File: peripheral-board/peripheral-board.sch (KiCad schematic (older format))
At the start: 12 parts, among them CON1001 AVR-ISP-10, P1001 Peripheral Bus, P1002 Power, SW1001 Power, U1001 ATTINY48-A

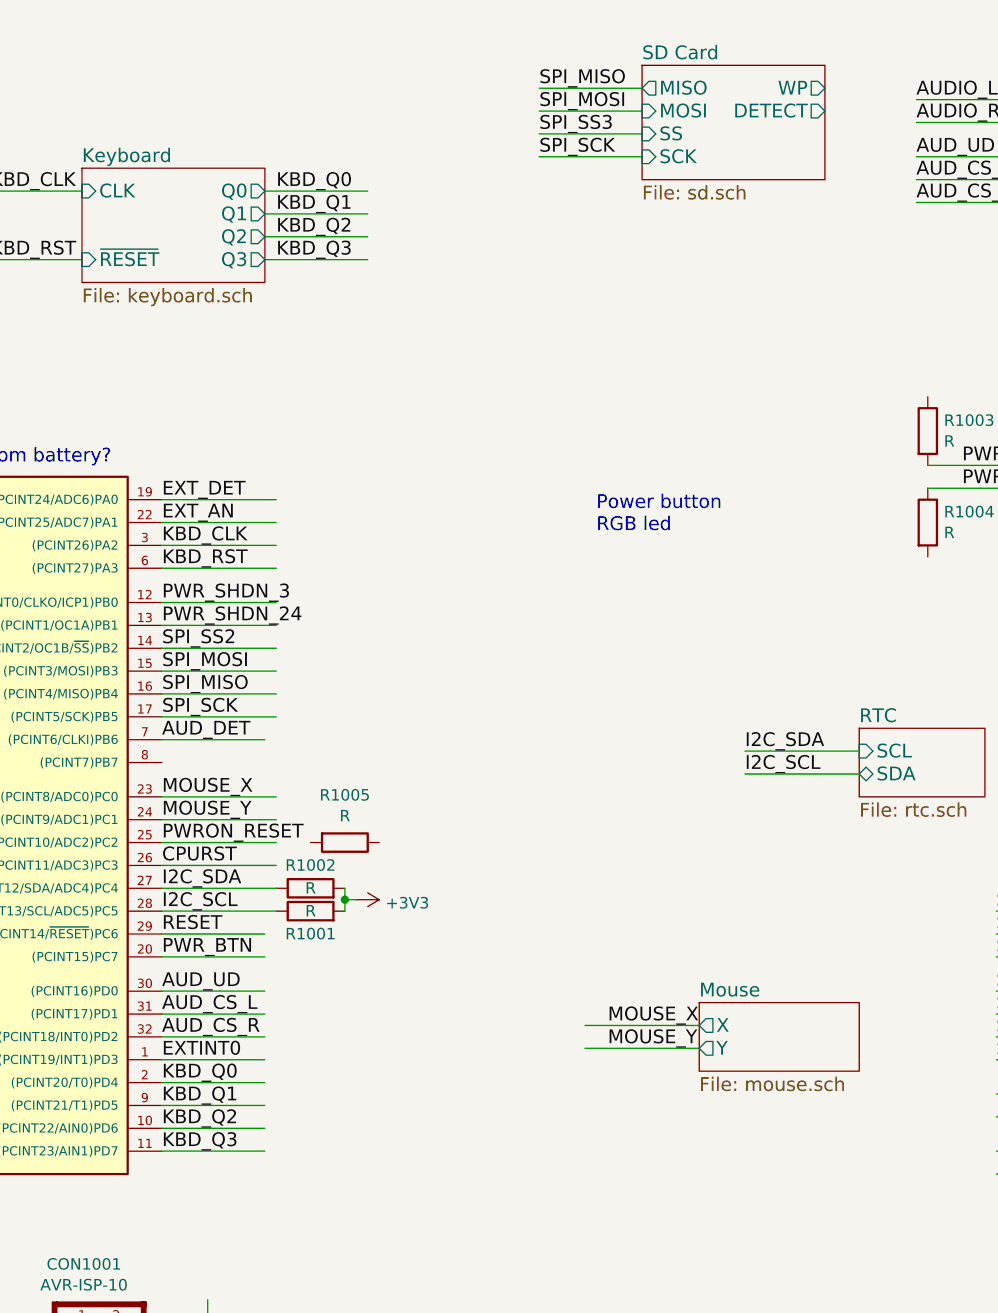
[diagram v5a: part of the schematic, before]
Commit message: audio components placement
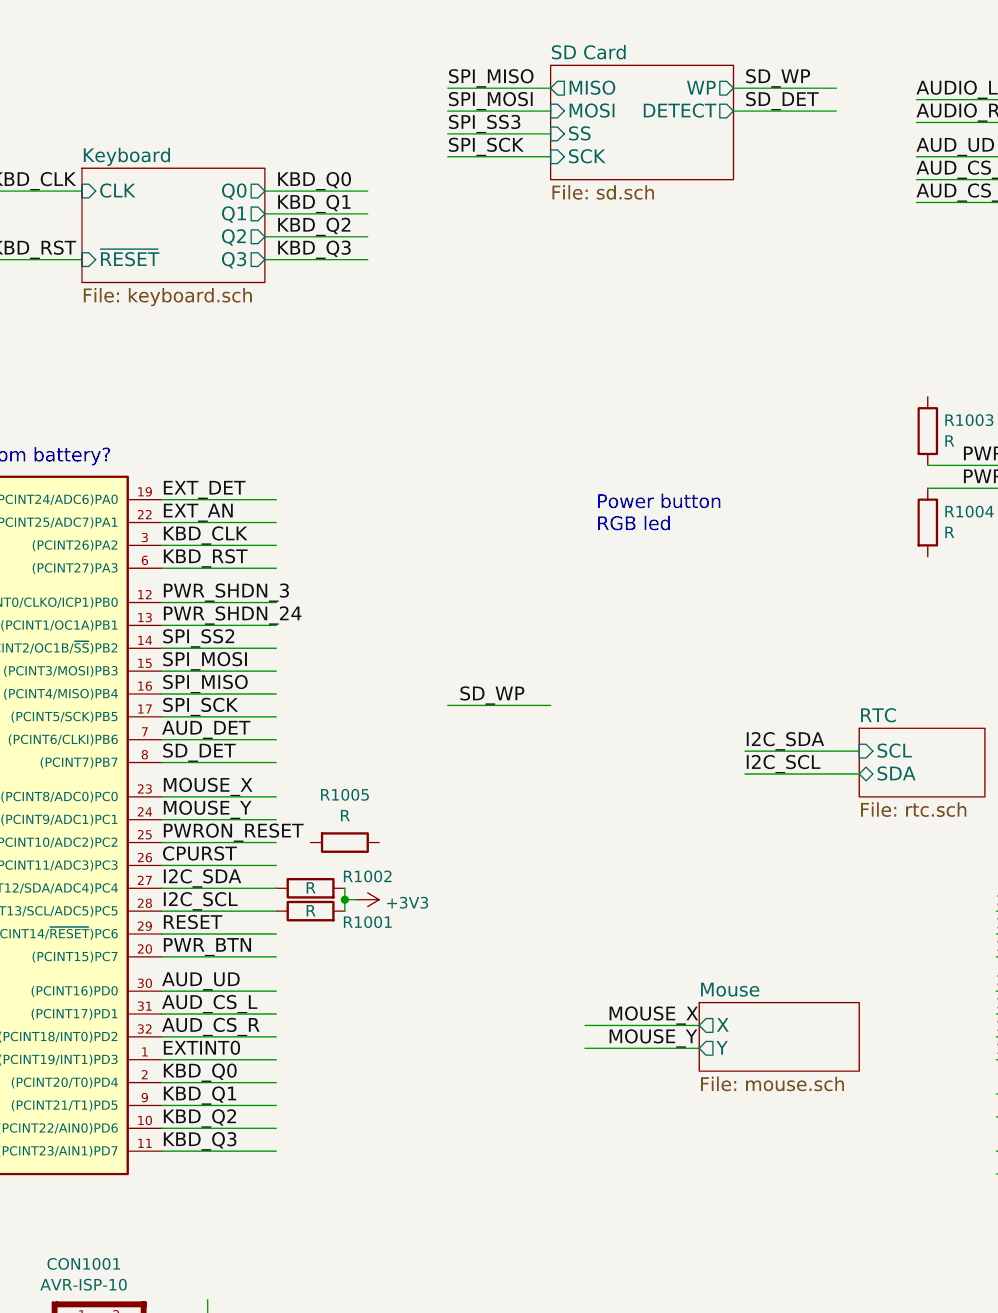
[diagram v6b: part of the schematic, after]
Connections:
- net labels added: SD_DET, SD_WP
- wire segments 126 -> 130
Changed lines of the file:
@@
 SPI_SCK
 $Comp
-L GND #PWR1014
+L GND #PWR01
 U 1 1 581F4F29
 P 5150 6850
-F 0 "#PWR1014" H 5150 6600 50  0001 C CNN
+F 0 "#PWR01" H 5150 6600 50  0001 C CNN
 F 1 "GND" H 5155 6677 50  0000 C CNN
 F 2 "" H 5150 6850 50  0000 C CNN
@@
 NoConn ~ 4550 6500
 $Comp
-L GND #PWR1011
+L GND #PWR02
 U 1 1 581F524B
 P 3000 5700
-F 0 "#PWR1011" H 3000 5450 50  0001 C CNN
+F 0 "#PWR02" H 3000 5450 50  0001 C CNN
 F 1 "GND" H 3005 5527 50  0000 C CNN
 F 2 "" H 3000 5700 50  0000 C CNN
@@
 SPI_SS7
 $Comp
-L GND #PWR1001
+L GND #PWR03
 U 1 1 581F752E
 P 1000 1950
-F 0 "#PWR1001" H 1000 1700 50  0001 C CNN
+F 0 "#PWR03" H 1000 1700 50  0001 C CNN
 F 1 "GND" V 1005 1822 50  0000 R CNN
 F 2 "" H 1000 1950 50  0000 C CNN
@@
 $EndComp
 $Comp
-L GND #PWR1002
+L GND #PWR04
 U 1 1 581F7634
 P 1000 2800
-F 0 "#PWR1002" H 1000 2550 50  0001 C CNN
+F 0 "#PWR04" H 1000 2550 50  0001 C CNN
 F 1 "GND" V 1005 2672 50  0000 R CNN
 F 2 "" H 1000 2800 50  0000 C CNN
@@
 $EndComp
 $Comp
-L GND #PWR1003
+L GND #PWR05
 U 1 1 581F76B8
 P 1000 3200
-F 0 "#PWR1003" H 1000 2950 50  0001 C CNN
+F 0 "#PWR05" H 1000 2950 50  0001 C CNN
 F 1 "GND" V 1005 3072 50  0000 R CNN
 F 2 "" H 1000 3200 50  0000 C CNN
@@
 $EndComp
 $Comp
-L GND #PWR1004
+L GND #PWR06
 U 1 1 581F7709
 P 1000 3500
-F 0 "#PWR1004" H 1000 3250 50  0001 C CNN
+F 0 "#PWR06" H 1000 3250 50  0001 C CNN
 F 1 "GND" V 1005 3372 50  0000 R CNN
 F 2 "" H 1000 3500 50  0000 C CNN
@@
 $EndComp
 $Comp
-L GND #PWR1005
+L GND #PWR07
 U 1 1 581F7744
 P 1000 4200
-F 0 "#PWR1005" H 1000 3950 50  0001 C CNN
+F 0 "#PWR07" H 1000 3950 50  0001 C CNN
 F 1 "GND" V 1005 4072 50  0000 R CNN
 F 2 "" H 1000 4200 50  0000 C CNN
@@
 $EndComp
 $Comp
-L GND #PWR1006
+L GND #PWR08
 U 1 1 581F77D7
 P 1000 4450
-F 0 "#PWR1006" H 1000 4200 50  0001 C CNN
+F 0 "#PWR08" H 1000 4200 50  0001 C CNN
 F 1 "GND" V 1005 4322 50  0000 R CNN
 F 2 "" H 1000 4450 50  0000 C CNN
@@
 $EndComp
 $Comp
-L GND #PWR1009
+L GND #PWR09
 U 1 1 581F7812
 P 1000 4950
-F 0 "#PWR1009" H 1000 4700 50  0001 C CNN
+F 0 "#PWR09" H 1000 4700 50  0001 C CNN
 F 1 "GND" V 1005 4822 50  0000 R CNN
 F 2 "" H 1000 4950 50  0000 C CNN
@@
 $EndComp
 $Comp
-L +24V #PWR1008
+L +24V #PWR010
 U 1 1 581F7F97
 P 1000 4800
-F 0 "#PWR1008" H 1000 4650 50  0001 C CNN
+F 0 "#PWR010" H 1000 4650 50  0001 C CNN
 F 1 "+24V" V 1000 4950 50  0000 L CNN
 F 2 "" H 1000 4800 50  0000 C CNN
@@
 $EndComp
 $Comp
-L +3V3 #PWR1010
+L +3V3 #PWR011
 U 1 1 581F7FED
 P 1000 5100
-F 0 "#PWR1010" H 1000 4950 50  0001 C CNN
+F 0 "#PWR011" H 1000 4950 50  0001 C CNN
 F 1 "+3V3" V 1000 5250 50  0000 L CNN
 F 2 "" H 1000 5100 50  0000 C CNN
@@
 $EndComp
 $Sheet
-S 7050 900  800  500
+S 6650 900  800  500
 U 581F67DF
 F0 "SD Card" 60
 F1 "sd.sch" 60
-F2 "MISO" O L 7050 1000 60
-F3 "MOSI" I L 7050 1100 60
-F4 "SS" I L 7050 1200 60
-F5 "SCK" I L 7050 1300 60
-F6 "WP" O R 7850 1000 60
-F7 "DETECT" O R 7850 1100 60
+F2 "MISO" O L 6650 1000 60
+F3 "MOSI" I L 6650 1100 60
+F4 "SS" I L 6650 1200 60
+F5 "SCK" I L 6650 1300 60
+F6 "WP" O R 7450 1000 60
+F7 "DETECT" O R 7450 1100 60
 $EndSheet
 $Comp
@@
 $EndComp
 $Comp
-L GND #PWR1013
+L GND #PWR012
 U 1 1 581F76DB
 P 2700 6850
-F 0 "#PWR1013" H 2700 6600 50  0001 C CNN
+F 0 "#PWR012" H 2700 6600 50  0001 C CNN
 F 1 "GND" H 2705 6677 50  0000 C CNN
 F 2 "" H 2700 6850 50  0000 C CNN
@@
 $EndComp
 $Comp
-L +3V3 #PWR1012
+L +3V3 #PWR013
 U 1 1 581F7984
 P 2700 6400
-F 0 "#PWR1012" H 2700 6250 50  0001 C CNN
+F 0 "#PWR013" H 2700 6250 50  0001 C CNN
 F 1 "+3V3" H 2715 6573 50  0000 C CNN
 F 2 "" H 2700 6400 50  0000 C CNN
@@
 U 1 1 58224307
 P 5600 4600
-F 0 "R1001" V 5500 4600 50  0000 C CNN
+F 0 "R1001" V 5550 4350 50  0000 C CNN
 F 1 "R" V 5600 4600 50  0000 C CNN
 F 2 "Resistors_SMD:R_0805" V 5530 4600 50  0001 C CNN
@@
 U 1 1 582244B8
 P 5600 4500
-F 0 "R1002" V 5700 4500 50  0000 C CNN
+F 0 "R1002" V 5650 4250 50  0000 C CNN
 F 1 "R" V 5600 4500 50  0000 C CNN
 F 2 "Resistors_SMD:R_0805" V 5530 4500 50  0001 C CNN
@@
 I2C_SCL
 $Comp
-L +3V3 #PWR1007
+L +3V3 #PWR014
 U 1 1 58A469F7
 P 5800 4550
-F 0 "#PWR1007" H 5850 4600 50  0001 C CNN
+F 0 "#PWR014" H 5850 4600 50  0001 C CNN
 F 1 "+3V3" V 5815 4678 50  0000 L CNN
 F 2 "" H -500 0   50  0001 C CNN
@@
 Text Label 4200 1750 0    60   ~ 0
 KBD_RST
-Text Label 6600 1100 0    60   ~ 0
+Text Label 6200 1100 0    60   ~ 0
 SPI_MOSI
-Text Label 6600 1000 0    60   ~ 0
+Text Label 6200 1000 0    60   ~ 0
 SPI_MISO
-Text Label 6600 1300 0    60   ~ 0
+Text Label 6200 1300 0    60   ~ 0
 SPI_SCK
 Wire Wire Line
-	6600 1000 7050 1000
-Wire Wire Line
-	6600 1100 7050 1100
-Wire Wire Line
-	6600 1200 7050 1200
-Wire Wire Line
-	6600 1300 7050 1300
+	6200 1000 6650 1000
+Wire Wire Line
+	6200 1100 6650 1100
+Wire Wire Line
+	6200 1200 6650 1200
+Wire Wire Line
+	6200 1300 6650 1300
 Text Label 8600 4700 0    60   ~ 0
 SPI_MOSI
@@
 Text Label 8600 5500 0    60   ~ 0
 UART_RX
-Text Label 6600 1200 0    60   ~ 0
+Text Label 6200 1200 0    60   ~ 0
 SPI_SS3
 Text Label 8600 4950 0    60   ~ 0
@@
 Text Label 8250 1500 0    60   ~ 0
 AUD_CS_R
-Wire Wire Line
-	4950 4950 5400 4950
-Wire Wire Line
-	5400 5050 4950 5050
-Wire Wire Line
-	5400 5150 4950 5150
 Text Label 4950 4950 0    60   ~ 0
 AUD_UD
@@
 Wire Wire Line
 	5450 3100 4950 3100
-Wire Wire Line
-	4950 5350 5400 5350
-Wire Wire Line
-	4950 5450 5400 5450
-Wire Wire Line
-	4950 5550 5400 5550
-Wire Wire Line
-	4950 5650 5400 5650
 Text Label 4950 5350 0    60   ~ 0
 KBD_Q0
@@
 Text Label 10400 4600 0    60   ~ 0
 EXTINT1
-Wire Wire Line
-	4950 5250 5400 5250
 Text Label 4950 4800 0    60   ~ 0
 PWR_BTN
-Wire Wire Line
-	4950 4800 5400 4800
 Text Label 4950 3250 0    60   ~ 0
 PWR_SHDN_3
@@
 Text Label 9450 1050 0    60   ~ 0
 AUD_DET
-Wire Wire Line
-	4950 3850 5400 3850
 Text Label 4950 3850 0    60   ~ 0
 AUD_DET
@@
 RESET
 Wire Wire Line
-	4950 4700 5400 4700
+	7450 1000 7900 1000
+Wire Wire Line
+	7450 1100 7900 1100
+Text Label 7500 1000 0    60   ~ 0
+SD_WP
+Text Label 7500 1100 0    60   ~ 0
+SD_DET
+Wire Wire Line
+	6200 3700 6650 3700
+Text Label 6250 3700 0    60   ~ 0
+SD_WP
+Text Label 4950 3950 0    60   ~ 0
+SD_DET
+Wire Wire Line
+	4950 3850 5450 3850
+Wire Wire Line
+	4950 4700 5450 4700
+Wire Wire Line
+	4950 4800 5450 4800
+Wire Wire Line
+	4950 4950 5450 4950
+Wire Wire Line
+	4950 5050 5450 5050
+Wire Wire Line
+	4950 5150 5450 5150
+Wire Wire Line
+	4950 5250 5450 5250
+Wire Wire Line
+	4950 5350 5450 5350
+Wire Wire Line
+	4950 5450 5450 5450
+Wire Wire Line
+	4950 5550 5450 5550
+Wire Wire Line
+	4950 5650 5450 5650
+Wire Wire Line
+	4950 3950 5450 3950
 $EndSCHEMATC

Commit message: routed spi
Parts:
- removed D1001: Status LED, symbol LED_RABG
- added D1001: LED_PWR, LEDs:LED-3MM, symbol LED
- added R1006: 1k, Resistors_SMD:R_0805, symbol R
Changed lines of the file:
@@
 	1    0    0    -1
-$EndComp
-$Comp
-L LED_RABG D1001
-U 1 1 582399DC
-P 3350 1250
-F 0 "D1001" V 3396 922 50  0000 R CNN
-F 1 "Status LED" V 3305 922 50  0000 R CNN
-F 2 "" H 3300 1200 50  0001 C CNN
-F 3 "" H 3300 1200 50  0000 C CNN
-	1    3350 1250
-	0    -1   -1   0
 $EndComp
 Text Notes 2800 800  0    60   ~ 0
@@
 Wire Wire Line
 	4950 3950 5450 3950
+$Comp
+L LED D1001
+U 1 1 58A4D1EF
+P 3250 1300
+F 0 "D1001" V 3288 1182 50  0000 R CNN
+F 1 "LED_PWR" V 3197 1182 50  0000 R CNN
+F 2 "LEDs:LED-3MM" H -50 -750 50  0001 C CNN
+F 3 "" H -50 -750 50  0001 C CNN
+	1    3250 1300
+	0    -1   -1   0
+$EndComp
+$Comp
+L R R1006
+U 1 1 58A4D893
+P 3250 1600
+F 0 "R1006" H 3320 1646 50  0000 L CNN
+F 1 "1k" H 3320 1555 50  0000 L CNN
+F 2 "Resistors_SMD:R_0805" V -170 -400 50  0001 C CNN
+F 3 "" H -100 -400 50  0001 C CNN
+	1    3250 1600
+	1    0    0    -1
+$EndComp
+$Comp
+L GND #PWR015
+U 1 1 58A4D9DD
+P 3250 1750
+F 0 "#PWR015" H -50 -250 50  0001 C CNN
+F 1 "GND" H 3255 1577 50  0000 C CNN
+F 2 "" H -50 0   50  0001 C CNN
+F 3 "" H -50 0   50  0001 C CNN
+	1    3250 1750
+	1    0    0    -1
+$EndComp
+$Comp
+L +3V3 #PWR016
+U 1 1 58A4DB27
+P 3250 1150
+F 0 "#PWR016" H -200 -800 50  0001 C CNN
+F 1 "+3V3" H 3265 1323 50  0000 C CNN
+F 2 "" H -200 -650 50  0001 C CNN
+F 3 "" H -200 -650 50  0001 C CNN
+	1    3250 1150
+	1    0    0    -1
+$EndComp
 $EndSCHEMATC

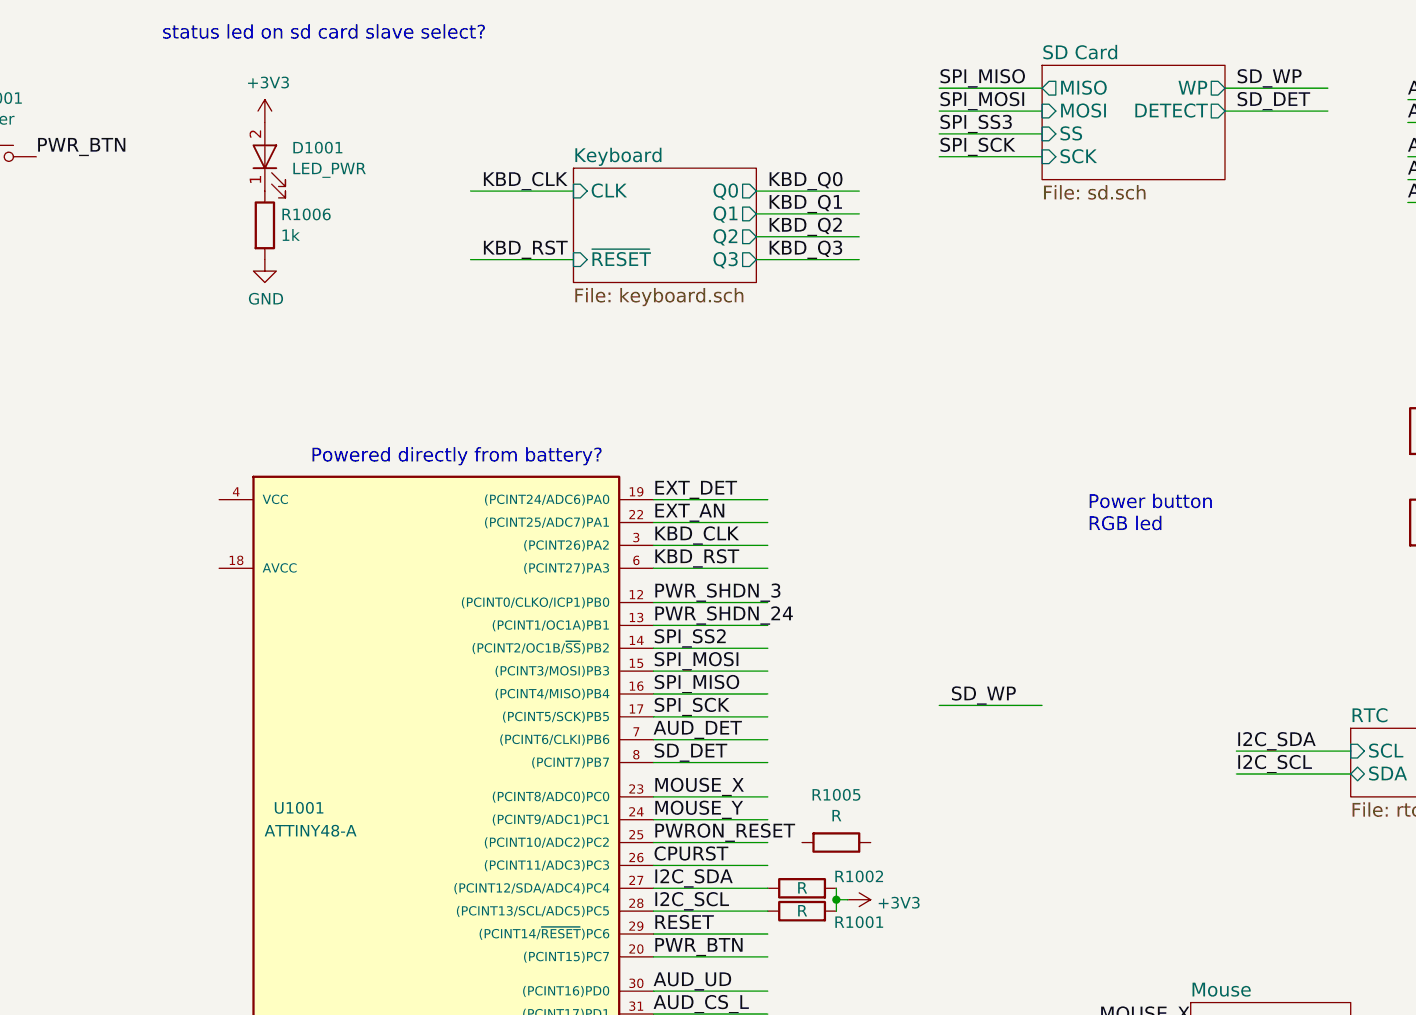
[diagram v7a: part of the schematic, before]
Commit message: routed audio circuitry
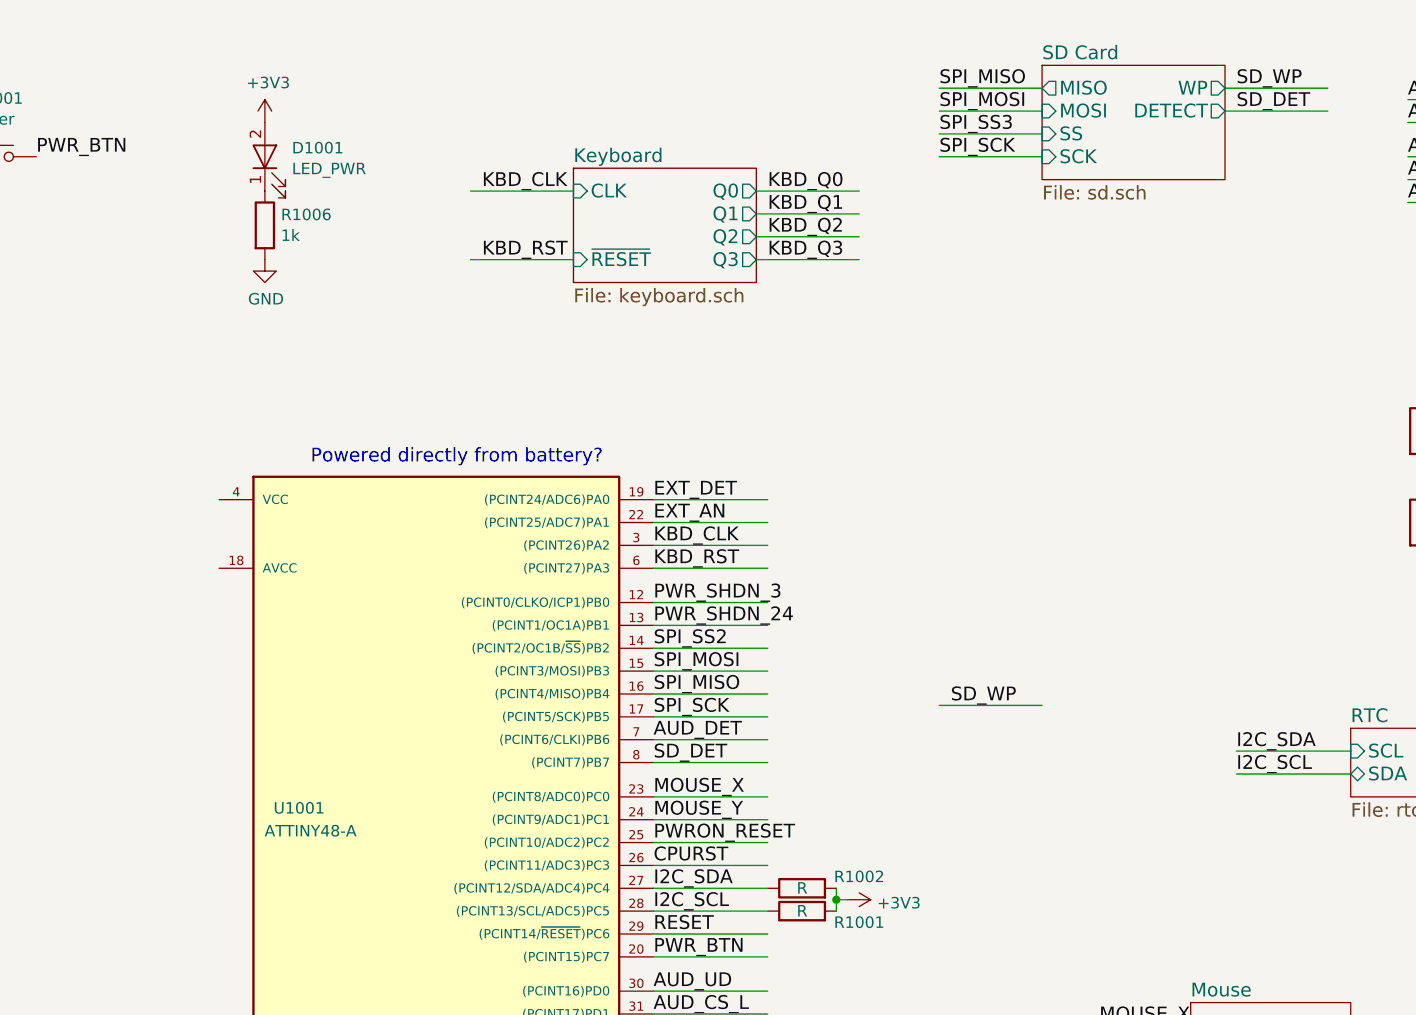
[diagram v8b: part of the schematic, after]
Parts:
- removed R1005: R, Resistors_SMD:R_0805, symbol R
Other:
- note removed: "Power button\nRGB led"
- note removed: "status led on sd card slave select?"
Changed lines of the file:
@@
 F1 "vga.sch" 60
 $EndSheet
-Text Notes 6850 2950 0    60   ~ 0
-Power button\nRGB led
 $Comp
 L R R1001
@@
 	1    0    0    -1
 $EndComp
-Text Notes 2800 800  0    60   ~ 0
-status led on sd card slave select?
 Text Label 10400 5750 0    60   ~ 0
 EXT_AN
@@
 Wire Wire Line
 	4950 4400 5450 4400
-$Comp
-L R R1005
-U 1 1 58A7B843
-P 5750 4300
-F 0 "R1005" V 5543 4300 50  0000 C CNN
-F 1 "R" V 5634 4300 50  0000 C CNN
-F 2 "Resistors_SMD:R_0805" V -270 450 50  0001 C CNN
-F 3 "" H -200 450 50  0001 C CNN
-	1    5750 4300
-	0    1    1    0
-$EndComp
 NoConn ~ 1400 1800
 NoConn ~ 1400 2100
